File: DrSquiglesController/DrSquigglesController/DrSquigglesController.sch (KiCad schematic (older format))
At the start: 7 parts, among them J1 Conn_01x04, J2 Conn_01x02, J3 Conn_02x08_Odd_Even, J4 Screw_Terminal_01x02, U1 teensy_3_2, U2 D24V22F5, U3 ULN2803A

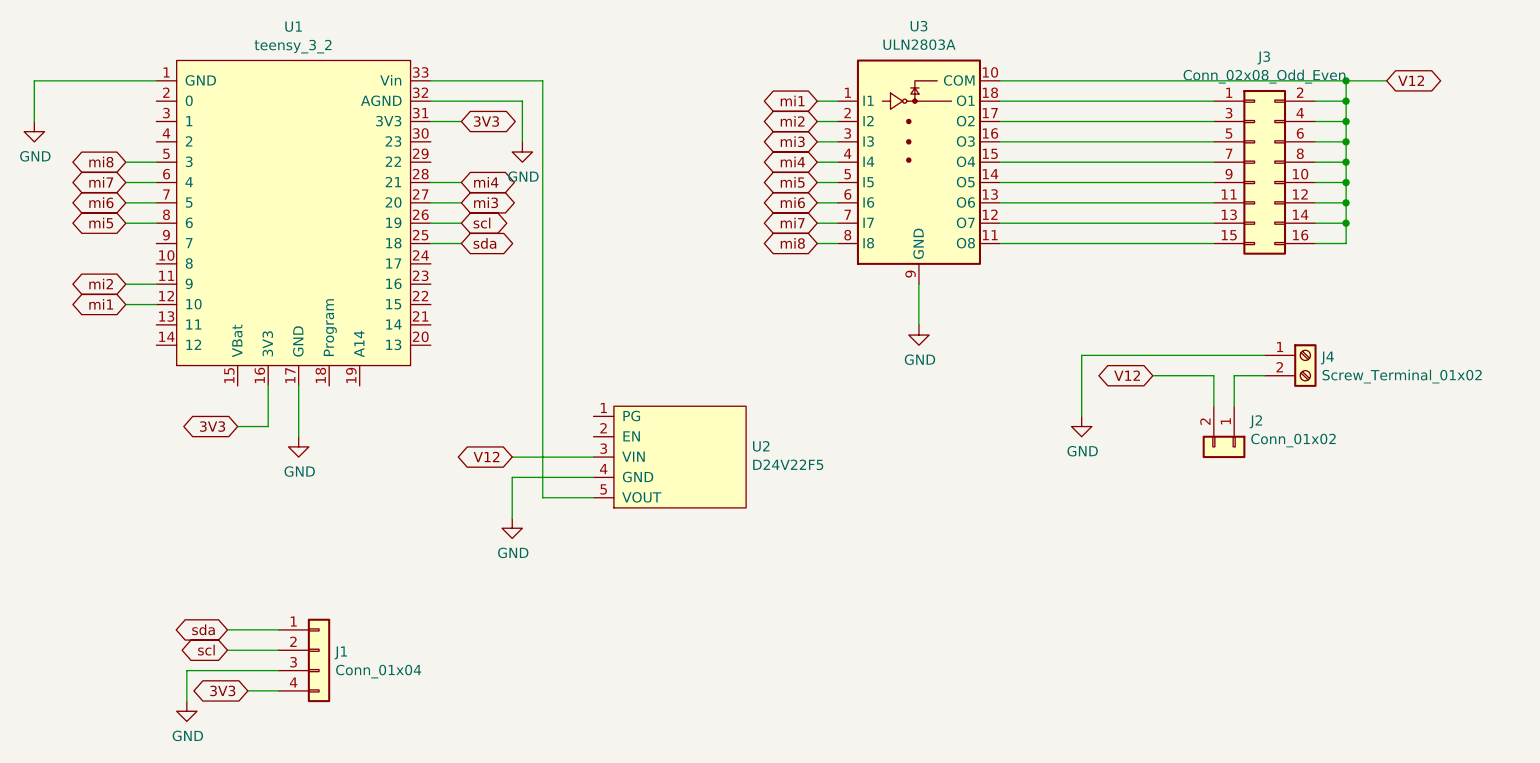
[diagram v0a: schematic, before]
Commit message: added jumper for raspi power
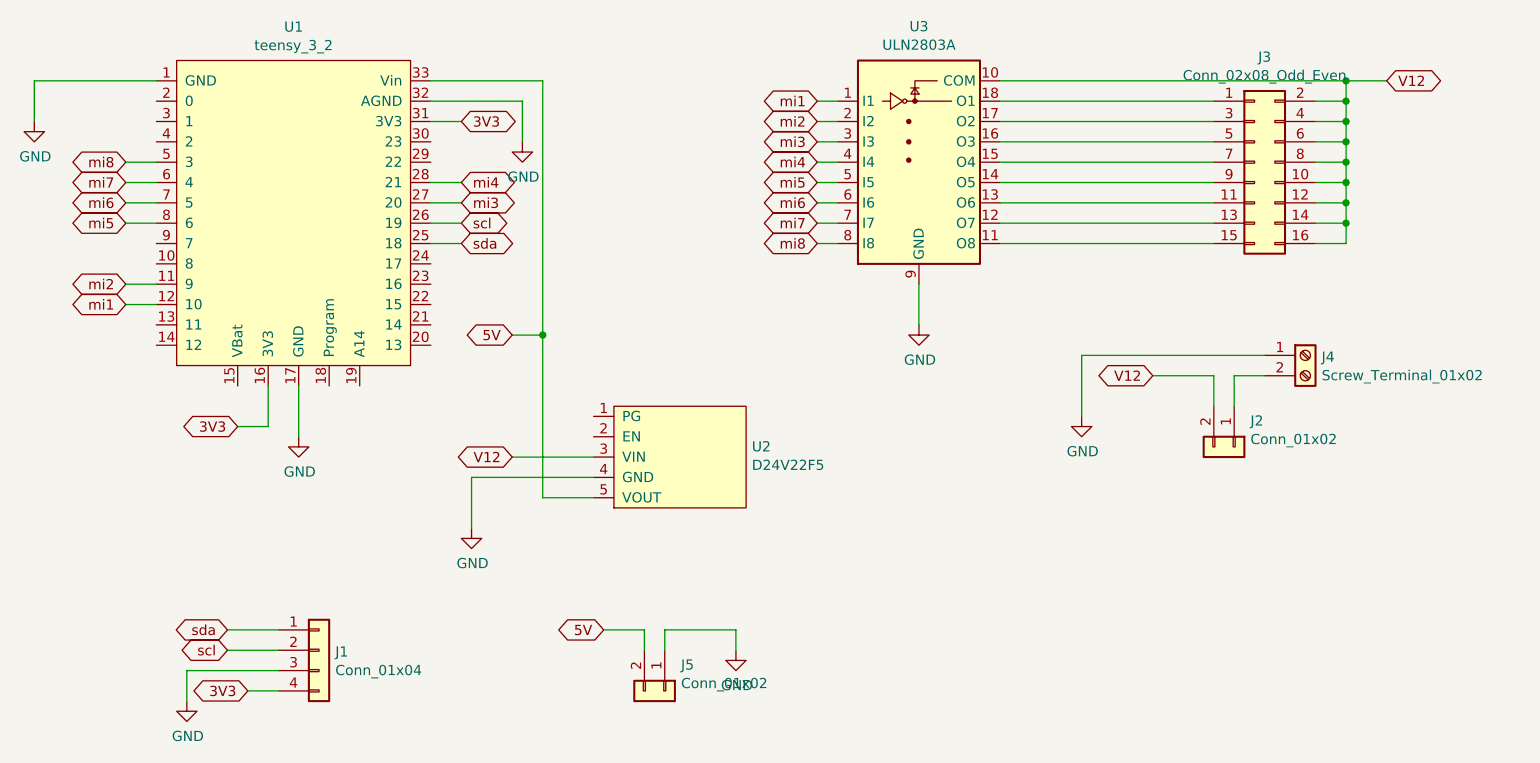
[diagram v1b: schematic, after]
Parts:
- added J5: Conn_01x02, Connector_PinHeader_2.54mm:PinHeader_1x02_P2.54mm_Vertical, symbol Connector_Generic:Conn_01x02
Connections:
- net GND: now also J5.1 (Pin_1)
- net 5V: now reaches U1.33 (Vin), U2.5 (VOUT)
- net 5V: now also J5.2 (Pin_2)
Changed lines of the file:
@@
 L power:GND #PWR0103
 U 1 1 5E8B1D08
-P 5650 4800
-F 0 "#PWR0103" H 5650 4550 50  0001 C CNN
-F 1 "GND" H 5655 4627 50  0000 C CNN
-F 2 "" H 5650 4800 50  0001 C CNN
-F 3 "" H 5650 4800 50  0001 C CNN
-	1    5650 4800
+P 5450 4850
+F 0 "#PWR0103" H 5450 4600 50  0001 C CNN
+F 1 "GND" H 5455 4677 50  0000 C CNN
+F 2 "" H 5450 4850 50  0001 C CNN
+F 3 "" H 5450 4850 50  0001 C CNN
+	1    5450 4850
 	1    0    0    -1
 $EndComp
@@
 	7650 3650 7650 3850
 Wire Wire Line
-	6050 4600 5650 4600
-Wire Wire Line
-	5650 4600 5650 4800
-Wire Wire Line
 	5250 2650 5800 2650
 Wire Wire Line
-	5800 2650 5800 4700
+	5800 2650 5800 3900
 Wire Wire Line
 	5800 4700 6050 4700
@@
 Wire Wire Line
 	8800 4100 9100 4100
+$Comp
+L Connector_Generic:Conn_01x02 J5
+U 1 1 5E8CAC1C
+P 6400 5650
+F 0 "J5" V 6272 5730 50  0000 L CNN
+F 1 "Conn_01x02" V 6363 5730 50  0000 L CNN
+F 2 "Connector_PinHeader_2.54mm:PinHeader_1x02_P2.54mm_Vertical" H 6400 5650 50  0001 C CNN
+F 3 "~" H 6400 5650 50  0001 C CNN
+	1    6400 5650
+	0    1    1    0
+$EndComp
+Wire Wire Line
+	5450 4600 6050 4600
+Wire Wire Line
+	5450 4600 5450 4850
+Text GLabel 5650 3900 0    50   BiDi ~ 0
+5V
+Wire Wire Line
+	5650 3900 5800 3900
+Connection ~ 5800 3900
+Wire Wire Line
+	5800 3900 5800 4700
+Text GLabel 6100 5350 0    50   BiDi ~ 0
+5V
+Wire Wire Line
+	6300 5350 6300 5450
+Wire Wire Line
+	6100 5350 6300 5350
+$Comp
+L power:GND #PWR0108
+U 1 1 5E8D54DC
+P 6750 5450
+F 0 "#PWR0108" H 6750 5200 50  0001 C CNN
+F 1 "GND" H 6755 5277 50  0000 C CNN
+F 2 "" H 6750 5450 50  0001 C CNN
+F 3 "" H 6750 5450 50  0001 C CNN
+	1    6750 5450
+	1    0    0    -1
+$EndComp
+Wire Wire Line
+	6750 5450 6750 5350
+Wire Wire Line
+	6750 5350 6400 5350
+Wire Wire Line
+	6400 5350 6400 5450
 $EndSCHEMATC
